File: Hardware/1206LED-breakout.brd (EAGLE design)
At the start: 15 x 15 mm, 5 parts

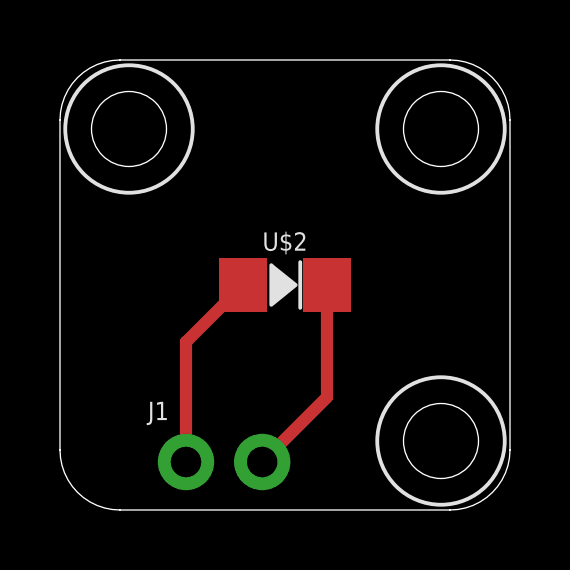
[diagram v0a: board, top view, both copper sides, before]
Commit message: Updated breakouts and main board, schematic v0.1 updates
Updated schematic for main unit to v0.1, incorporating updates from testing of v0.0 unit
Minor updates to breakout boards, adding passives and updating components
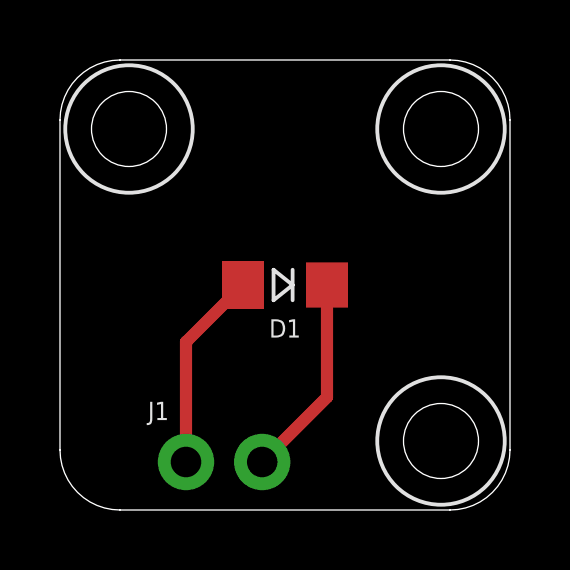
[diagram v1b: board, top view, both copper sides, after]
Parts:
- removed U$2: 1206-LED, bschulz:1206-LED
- added D1: LED1206, bschulz:LED_1206
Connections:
- net ANODE: now also D1.ANODE; no longer U$2.ANODE
- net CATHODE: now also D1.CATHODE; no longer U$2.CATHODE
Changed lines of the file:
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@@
 <?xml version="1.0" encoding="utf-8"?>
 <!DOCTYPE eagle SYSTEM "eagle.dtd">
-<eagle version="9.2.0">
+<eagle version="9.1.3">
 <drawing>
 <settings>
@@
 <layers>
 <layer number="1" name="Top" color="4" fill="1" visible="yes" active="yes"/>
+<layer number="2" name="Route2" color="1" fill="3" visible="no" active="no"/>
+<layer number="3" name="Route3" color="4" fill="3" visible="no" active="no"/>
+<layer number="4" name="Route4" color="1" fill="4" visible="no" active="no"/>
+<layer number="5" name="Route5" color="4" fill="4" visible="no" active="no"/>
+<layer number="6" name="Route6" color="1" fill="8" visible="no" active="no"/>
+<layer number="7" name="Route7" color="4" fill="8" visible="no" active="no"/>
+<layer number="8" name="Route8" color="1" fill="2" visible="no" active="no"/>
+<layer number="9" name="Route9" color="4" fill="2" visible="no" active="no"/>
+<layer number="10" name="Route10" color="1" fill="7" visible="no" active="no"/>
+<layer number="11" name="Route11" color="4" fill="7" visible="no" active="no"/>
+<layer number="12" name="Route12" color="1" fill="5" visible="no" active="no"/>
+<layer number="13" name="Route13" color="4" fill="5" visible="no" active="no"/>
+<layer number="14" name="Route14" color="1" fill="6" visible="no" active="no"/>
+<layer number="15" name="Route15" color="4" fill="6" visible="no" active="no"/>
 <layer number="16" name="Bottom" color="1" fill="1" visible="yes" active="yes"/>
 <layer number="17" name="Pads" color="2" fill="1" visible="yes" active="yes"/>
@@
 <wire x1="0" y1="13" x2="0" y2="2" width="0" layer="20"/>
 <wire x1="0" y1="2" x2="2" y2="0" width="0" layer="20" curve="90"/>
-<text x="3.8" y="2.9" size="0.8128" layer="52" rot="MR90">Anode (+)</text>
-<text x="6.3" y="2.9" size="0.8128" layer="52" rot="MR90">Cathode (-)</text>
+<text x="3.8" y="2.9" size="0.8128" layer="52" font="vector" ratio="15" rot="MR90">Anode (+)</text>
+<text x="6.3" y="2.9" size="0.8128" layer="52" font="vector" ratio="15" rot="MR90">Cathode (-)</text>
 </plain>
 <attributes>
@@
 <element name="H2" library="bschulz" package="2_56" value="" x="12.7" y="2.3"/>
 <element name="H3" library="bschulz" package="2_56" value="" x="12.7" y="12.7"/>
-<element name="U$2" library="bschulz" package="1206-LED" value="1206-LED" x="7.5" y="7.5">
-<attribute name="NAME" x="7.5" y="8.643" size="0.6096" layer="25" font="vector" ratio="20" align="bottom-center"/>
-<attribute name="VALUE" x="7.5" y="6.357" size="0.6096" layer="27" font="vector" ratio="20" align="top-center"/>
+<element name="D1" library="bschulz" package="LED_1206" value="LED1206" x="7.5" y="7.5" smashed="yes" rot="R180">
+<attribute name="NAME" x="7.5" y="6.357" size="0.6096" layer="25" font="vector" ratio="20" rot="R180" align="bottom-center"/>
+<attribute name="VALUE" x="7.5" y="8.77" size="0.6096" layer="27" font="vector" ratio="20" rot="R180" align="top-center"/>
 </element>
 <element name="J1" library="bschulz" package="1X02_NO_SILK" value="" x="4.2" y="1.6">
@@
 <signals>
 <signal name="ANODE">
-<contactref element="U$2" pad="ANODE"/>
+<contactref element="D1" pad="ANODE"/>
 <contactref element="J1" pad="1"/>
 <wire x1="6.1" y1="7.5" x2="4.2" y2="5.6" width="0.4064" layer="1"/>
@@
 </signal>
 <signal name="CATHODE">
-<contactref element="U$2" pad="CATHODE"/>
+<contactref element="D1" pad="CATHODE"/>
 <contactref element="J1" pad="2"/>
 <wire x1="8.9" y1="7.5" x2="8.9" y2="3.76" width="0.4064" layer="1"/>
